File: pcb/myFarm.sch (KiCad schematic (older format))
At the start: 10 parts, among them J0 Conn_01x02, J1 LED, J2 SENSOR, J3 SW_LED, J4 RELAY, J5 POWER DRIVE, J6 JUMPER, J7 SW_LED, U1 WeMos_D1_mini, U2 MCP23017_MODULE

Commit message: update pcb
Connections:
- wire segments 80 -> 82
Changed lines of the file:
@@
 EESchema Schematic File Version 4
 LIBS:myFarm-cache
-EELAYER 29 0
+EELAYER 30 0
 EELAYER END
 $Descr A4 11693 8268
@@
 	3600 5400 3250 5400
 Wire Wire Line
-	3250 5500 3500 5500
-Wire Wire Line
 	3500 6300 3500 6050
 Wire Wire Line
@@
 	1650 4150 1650 2900
 Wire Wire Line
-	1650 2900 2800 2900
+	1650 2900 2150 2900
 Connection ~ 2800 2900
 Wire Wire Line
@@
 	3650 3250 3500 3250
 Wire Wire Line
-	3500 3250 3500 5500
-Connection ~ 3500 5500
-Wire Wire Line
-	3500 5500 3500 6050
-Wire Wire Line
 	3650 3050 3500 3050
 Wire Wire Line
@@
 	0    1    1    0
 $EndComp
+Wire Wire Line
+	3500 3250 3500 6050
+Wire Wire Line
+	3250 5500 3250 5750
+Wire Wire Line
+	3250 5750 2150 5750
+Wire Wire Line
+	2150 5750 2150 2900
+Connection ~ 2150 2900
+Wire Wire Line
+	2150 2900 2800 2900
 $EndSCHEMATC

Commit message: update pcb
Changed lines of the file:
@@
 	3100 3950 3250 3950
 Wire Wire Line
-	3250 3950 3250 5300
-Wire Wire Line
 	3850 4550 3600 4550
-Wire Wire Line
-	3600 4550 3600 5400
-Wire Wire Line
-	3600 5400 3250 5400
 Wire Wire Line
 	3500 6300 3500 6050
@@
 Wire Wire Line
 	1650 4150 1650 2900
-Wire Wire Line
-	1650 2900 2150 2900
 Connection ~ 2800 2900
 Wire Wire Line
@@
 	1550 2850 1550 4000
 Connection ~ 1550 4000
+Connection ~ 5900 3350
+Wire Wire Line
+	5900 3350 5900 3750
+Wire Wire Line
+	5900 3350 5900 3000
+Wire Wire Line
+	5650 3550 6300 3550
+Wire Wire Line
+	6300 3350 5900 3350
+Wire Wire Line
+	3500 3050 3500 2900
+Connection ~ 3500 2900
+Wire Wire Line
+	3500 2900 4550 2900
+$Comp
+L Connector_Generic:Conn_01x04 J7
+U 1 1 5D3E2091
+P 1550 4350
+F 0 "J7" V 1422 4530 50  0000 L CNN
+F 1 "SW_LED" V 1513 4530 50  0000 L CNN
+F 2 "Module:POWER_SUPPLY_MODULE" H 1550 4350 50  0001 C CNN
+F 3 "~" H 1550 4350 50  0001 C CNN
+	1    1550 4350
+	0    1    1    0
+$EndComp
+Wire Wire Line
+	3500 3250 3500 6050
+Wire Wire Line
+	3100 4150 3350 4150
+Wire Wire Line
+	3350 4150 3350 3150
+Wire Wire Line
+	3650 3050 3500 3050
+Wire Wire Line
+	3350 3150 3650 3150
+Wire Wire Line
+	3650 3250 3500 3250
 $Comp
 L Connector_Generic:Conn_01x03 J6
@@
 	-1   0    0    1
 $EndComp
-Connection ~ 5900 3350
-Wire Wire Line
-	5900 3350 5900 3750
-Wire Wire Line
-	5900 3350 5900 3000
-Wire Wire Line
-	5650 3550 6300 3550
-Wire Wire Line
-	6300 3350 5900 3350
+Wire Wire Line
+	3250 3950 3250 5300
+Wire Wire Line
+	3600 4550 3600 5400
+Wire Wire Line
+	3600 5400 3250 5400
+Wire Wire Line
+	3250 5500 3250 5750
+Wire Wire Line
+	3250 5750 2150 5750
+Wire Wire Line
+	2150 2900 2800 2900
+Wire Wire Line
+	1650 2900 2150 2900
+Connection ~ 2150 2900
+Wire Wire Line
+	2150 5750 2150 2900
 $Comp
 L Connector_Generic:Conn_01x03 J2
@@
 	1    0    0    -1
 $EndComp
-Wire Wire Line
-	3650 3250 3500 3250
-Wire Wire Line
-	3650 3050 3500 3050
-Wire Wire Line
-	3500 3050 3500 2900
-Connection ~ 3500 2900
-Wire Wire Line
-	3500 2900 4550 2900
-Wire Wire Line
-	3100 3650 3250 3650
-Wire Wire Line
-	3250 3650 3250 3150
-Wire Wire Line
-	3250 3150 3650 3150
-$Comp
-L Connector_Generic:Conn_01x04 J7
-U 1 1 5D3E2091
-P 1550 4350
-F 0 "J7" V 1422 4530 50  0000 L CNN
-F 1 "SW_LED" V 1513 4530 50  0000 L CNN
-F 2 "Module:POWER_SUPPLY_MODULE" H 1550 4350 50  0001 C CNN
-F 3 "~" H 1550 4350 50  0001 C CNN
-	1    1550 4350
-	0    1    1    0
-$EndComp
-Wire Wire Line
-	3500 3250 3500 6050
-Wire Wire Line
-	3250 5500 3250 5750
-Wire Wire Line
-	3250 5750 2150 5750
-Wire Wire Line
-	2150 5750 2150 2900
-Connection ~ 2150 2900
-Wire Wire Line
-	2150 2900 2800 2900
 $EndSCHEMATC

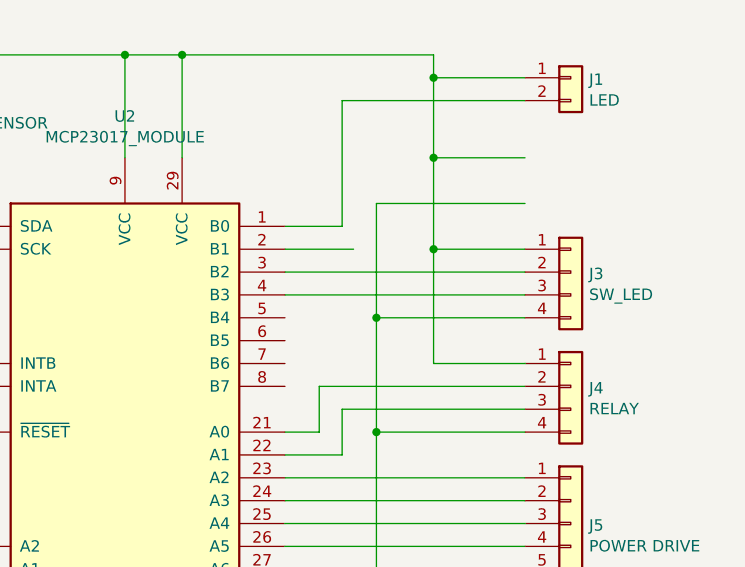
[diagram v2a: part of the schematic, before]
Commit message: swap connect j3
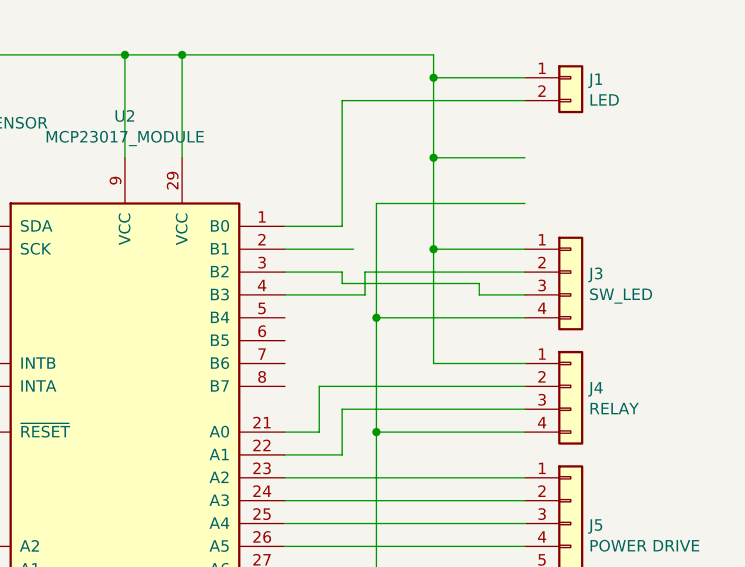
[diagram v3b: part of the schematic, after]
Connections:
- wire segments 82 -> 88
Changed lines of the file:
@@
 	5500 3100 6300 3100
-Wire Wire Line
-	5250 3850 6300 3850
-Wire Wire Line
-	5250 3950 6300 3950
 Wire Wire Line
 	5250 4550 5400 4550
@@
 	1    0    0    -1
 $EndComp
+Wire Wire Line
+	5250 3950 5600 3950
+Wire Wire Line
+	5600 3950 5600 3850
+Wire Wire Line
+	5600 3850 6300 3850
+Wire Wire Line
+	5250 3850 5500 3850
+Wire Wire Line
+	5500 3850 5500 3900
+Wire Wire Line
+	5500 3900 6100 3900
+Wire Wire Line
+	6100 3900 6100 3950
+Wire Wire Line
+	6100 3950 6300 3950
 $EndSCHEMATC

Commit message: update pcb
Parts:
- added J10: GENERAL, Connector_PinHeader_2.54mm:PinHeader_1x06_P2.54mm_Vertical, symbol Connector_Generic:Conn_01x06
- added J11: RXTX, Connector_PinHeader_2.54mm:PinHeader_1x02_P2.54mm_Vertical, symbol Connector_Generic:Conn_01x02
- added J12, J13, J14: VALVE OUT, Connector_PinHeader_2.54mm:PinHeader_1x02_P2.54mm_Vertical, symbol Connector_Generic:Conn_01x02
- added J8: Reset, Connector_PinHeader_2.54mm:PinHeader_1x02_P2.54mm_Vertical, symbol Connector_Generic:Conn_01x02
- added J9: VAVLE IN, Connector_PinHeader_2.54mm:PinHeader_1x02_P2.54mm_Vertical, symbol Connector_Generic:Conn_01x02
- added U3: DS1832S+, Package_DIP:DIP-8_W10.16mm, symbol DS1832S_:DS1832S+
- J0: value Conn_01x02 -> POWER
- J7: value SW_LED -> SUPPLY
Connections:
- wire segments 88 -> 150
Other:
- moved on the sheet: J0, J1, J2, J3, J4, J5, J6, J7, U1, U2

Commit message: update pcb.
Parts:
- added J15: SELECTOR, Connector_PinHeader_2.54mm:PinHeader_1x02_P2.54mm_Vertical, symbol Connector_Generic:Conn_01x02
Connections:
- net GNDREF: now also J15.1 (Pin_1)
- net at U1.11 (D4): now also J15.2 (Pin_2)
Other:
- moved on the sheet: J6
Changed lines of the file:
@@
 	5450 4500 5450 5700
 Wire Wire Line
-	5450 5700 6250 5700
+	5450 5700 6000 5700
 Wire Wire Line
 	7300 5200 7300 5700
@@
 Wire Wire Line
 	7300 2550 7550 2550
-Wire Wire Line
-	5850 3600 6000 3600
-Wire Wire Line
-	6600 4200 6350 4200
 Wire Wire Line
 	6250 5950 6250 5700
@@
 	8000 4900 9050 4900
 Connection ~ 5550 2550
-$Comp
-L Connector_Generic:Conn_01x03 J6
-U 1 1 5D3BA3DB
-P 5800 5050
-F 0 "J6" H 5718 4725 50  0000 C CNN
-F 1 "JUMPER" H 5718 4816 50  0000 C CNN
-F 2 "Connector_PinHeader_2.54mm:PinHeader_1x03_P2.54mm_Vertical" H 5800 5050 50  0001 C CNN
-F 3 "~" H 5800 5050 50  0001 C CNN
-	1    5800 5050
-	-1   0    0    1
-$EndComp
-Wire Wire Line
-	6350 4200 6350 5050
-Wire Wire Line
-	6350 5050 6000 5050
-Wire Wire Line
-	6000 5150 6000 5400
-Wire Wire Line
-	6000 5400 4900 5400
-Wire Wire Line
-	4900 2550 5550 2550
-Wire Wire Line
-	4900 5400 4900 2550
 Wire Wire Line
 	8000 3600 8350 3600
@@
 Wire Wire Line
 	3400 1700 4050 1700
-Connection ~ 4900 2550
 Wire Wire Line
 	4250 4250 4250 5700
@@
 Wire Wire Line
 	4250 3450 4250 2550
-Wire Wire Line
-	4250 2550 4900 2550
 Wire Wire Line
 	4400 3850 4400 3300
@@
 Wire Wire Line
 	3300 1700 3300 1850
-Wire Wire Line
-	6000 3600 6000 4950
 Wire Wire Line
 	5850 3900 6150 3900
@@
 	6850 2800 6850 1800
 Wire Wire Line
-	6550 3800 6550 2800
-Wire Wire Line
-	6550 2800 6850 2800
-Wire Wire Line
-	5850 3800 6550 3800
+	6450 3800 6450 2800
+Wire Wire Line
+	6450 2800 6850 2800
+Wire Wire Line
+	5850 3800 6450 3800
 Wire Wire Line
 	6000 1800 6000 3200
@@
 Connection ~ 6400 2550
 Wire Wire Line
-	6400 2550 6750 2550
+	6400 2550 6550 2550
 Wire Wire Line
 	6500 1800 6500 2200
@@
 	8650 2450 9050 2450
 $Comp
+L Connector_Generic:Conn_01x02 J9
+U 1 1 5D6744E9
+P 7700 1600
+F 0 "J9" H 7780 1592 50  0000 L CNN
+F 1 "VAVLE IN" H 7780 1501 50  0000 L CNN
+F 2 "Connector_PinHeader_2.54mm:PinHeader_1x02_P2.54mm_Vertical" H 7700 1600 50  0001 C CNN
+F 3 "~" H 7700 1600 50  0001 C CNN
+	1    7700 1600
+	0    -1   -1   0
+$EndComp
+$Comp
+L Connector_Generic:Conn_01x02 J12
+U 1 1 5D67486F
+P 8000 1600
+F 0 "J12" H 8080 1592 50  0000 L CNN
+F 1 "VALVE OUT" H 8080 1501 50  0000 L CNN
+F 2 "Connector_PinHeader_2.54mm:PinHeader_1x02_P2.54mm_Vertical" H 8000 1600 50  0001 C CNN
+F 3 "~" H 8000 1600 50  0001 C CNN
+	1    8000 1600
+	0    -1   -1   0
+$EndComp
+$Comp
+L Connector_Generic:Conn_01x02 J13
+U 1 1 5D6923CB
+P 8300 1600
+F 0 "J13" H 8380 1592 50  0000 L CNN
+F 1 "VALVE OUT" H 8380 1501 50  0000 L CNN
+F 2 "Connector_PinHeader_2.54mm:PinHeader_1x02_P2.54mm_Vertical" H 8300 1600 50  0001 C CNN
+F 3 "~" H 8300 1600 50  0001 C CNN
+	1    8300 1600
+	0    -1   -1   0
+$EndComp
+$Comp
+L Connector_Generic:Conn_01x02 J14
+U 1 1 5D692989
+P 8600 1600
+F 0 "J14" H 8680 1592 50  0000 L CNN
+F 1 "VALVE OUT" H 8680 1501 50  0000 L CNN
+F 2 "Connector_PinHeader_2.54mm:PinHeader_1x02_P2.54mm_Vertical" H 8600 1600 50  0001 C CNN
+F 3 "~" H 8600 1600 50  0001 C CNN
+	1    8600 1600
+	0    -1   -1   0
+$EndComp
+Wire Wire Line
+	8050 2100 7700 2100
+Wire Wire Line
+	7700 2100 7700 1800
+Wire Wire Line
+	8050 2100 8050 3700
+Wire Wire Line
+	8100 2000 8000 2000
+Wire Wire Line
+	8000 2000 8000 1800
+Wire Wire Line
+	8100 2000 8100 3800
+Wire Wire Line
+	8150 2000 8300 2000
+Wire Wire Line
+	8300 2000 8300 1800
+Wire Wire Line
+	8150 2000 8150 3900
+Wire Wire Line
+	8200 2100 8600 2100
+Wire Wire Line
+	8600 2100 8600 1800
+Wire Wire Line
+	8200 2100 8200 4000
+Wire Wire Line
+	7800 1800 7800 1950
+Wire Wire Line
+	7800 1950 8100 1950
+Wire Wire Line
+	8700 1950 8700 2200
+Wire Wire Line
+	8700 2200 8400 2200
+Connection ~ 8400 2200
+Wire Wire Line
+	8700 1800 8700 1950
+Connection ~ 8700 1950
+Wire Wire Line
+	8400 1800 8400 1950
+Connection ~ 8400 1950
+Wire Wire Line
+	8400 1950 8700 1950
+Wire Wire Line
+	8100 1800 8100 1950
+Connection ~ 8100 1950
+Wire Wire Line
+	8100 1950 8400 1950
+$Comp
+L Connector_Generic:Conn_01x03 J6
+U 1 1 5D3BA3DB
+P 6450 4500
+F 0 "J6" H 6368 4175 50  0000 C CNN
+F 1 "JUMPER" H 6368 4266 50  0000 C CNN
+F 2 "Connector_PinHeader_2.54mm:PinHeader_1x03_P2.54mm_Vertical" H 6450 4500 50  0001 C CNN
+F 3 "~" H 6450 4500 50  0001 C CNN
+	1    6450 4500
+	0    1    1    0
+$EndComp
+Wire Wire Line
+	6600 4200 6450 4200
+Wire Wire Line
+	6450 4200 6450 4300
+Wire Wire Line
+	6350 3600 6350 4300
+Wire Wire Line
+	6550 4300 6550 2550
+Connection ~ 6550 2550
+Wire Wire Line
+	6550 2550 6750 2550
+Wire Wire Line
+	5850 3600 6350 3600
+Wire Wire Line
+	4250 2550 5550 2550
+$Comp
+L Connector_Generic:Conn_01x02 J15
+U 1 1 5D75F2CC
+P 5700 5300
+F 0 "J15" H 5780 5292 50  0000 L CNN
+F 1 "SELECTOR" H 5780 5201 50  0000 L CNN
+F 2 "Connector_PinHeader_2.54mm:PinHeader_1x02_P2.54mm_Vertical" H 5700 5300 50  0001 C CNN
+F 3 "~" H 5700 5300 50  0001 C CNN
+	1    5700 5300
+	-1   0    0    1
+$EndComp
+Wire Wire Line
+	5850 3700 6000 3700
+Wire Wire Line
+	6000 3700 6000 5200
+Wire Wire Line
+	6000 5200 5900 5200
+Wire Wire Line
+	5900 5300 6000 5300
+Wire Wire Line
+	6000 5300 6000 5700
+Connection ~ 6000 5700
+Wire Wire Line
+	6000 5700 6250 5700
+$Comp
 L Connector_Generic:Conn_01x02 J1
 U 1 1 5D3273EB
@@
 	1    0    0    -1
 $EndComp
-$Comp
-L Connector_Generic:Conn_01x02 J9
-U 1 1 5D6744E9
-P 7700 1600
-F 0 "J9" H 7780 1592 50  0000 L CNN
-F 1 "VAVLE IN" H 7780 1501 50  0000 L CNN
-F 2 "Connector_PinHeader_2.54mm:PinHeader_1x02_P2.54mm_Vertical" H 7700 1600 50  0001 C CNN
-F 3 "~" H 7700 1600 50  0001 C CNN
-	1    7700 1600
-	0    -1   -1   0
-$EndComp
-$Comp
-L Connector_Generic:Conn_01x02 J12
-U 1 1 5D67486F
-P 8000 1600
-F 0 "J12" H 8080 1592 50  0000 L CNN
-F 1 "VALVE OUT" H 8080 1501 50  0000 L CNN
-F 2 "Connector_PinHeader_2.54mm:PinHeader_1x02_P2.54mm_Vertical" H 8000 1600 50  0001 C CNN
-F 3 "~" H 8000 1600 50  0001 C CNN
-	1    8000 1600
-	0    -1   -1   0
-$EndComp
-$Comp
-L Connector_Generic:Conn_01x02 J13
-U 1 1 5D6923CB
-P 8300 1600
-F 0 "J13" H 8380 1592 50  0000 L CNN
-F 1 "VALVE OUT" H 8380 1501 50  0000 L CNN
-F 2 "Connector_PinHeader_2.54mm:PinHeader_1x02_P2.54mm_Vertical" H 8300 1600 50  0001 C CNN
-F 3 "~" H 8300 1600 50  0001 C CNN
-	1    8300 1600
-	0    -1   -1   0
-$EndComp
-$Comp
-L Connector_Generic:Conn_01x02 J14
-U 1 1 5D692989
-P 8600 1600
-F 0 "J14" H 8680 1592 50  0000 L CNN
-F 1 "VALVE OUT" H 8680 1501 50  0000 L CNN
-F 2 "Connector_PinHeader_2.54mm:PinHeader_1x02_P2.54mm_Vertical" H 8600 1600 50  0001 C CNN
-F 3 "~" H 8600 1600 50  0001 C CNN
-	1    8600 1600
-	0    -1   -1   0
-$EndComp
-Wire Wire Line
-	8050 2100 7700 2100
-Wire Wire Line
-	7700 2100 7700 1800
-Wire Wire Line
-	8050 2100 8050 3700
-Wire Wire Line
-	8100 2000 8000 2000
-Wire Wire Line
-	8000 2000 8000 1800
-Wire Wire Line
-	8100 2000 8100 3800
-Wire Wire Line
-	8150 2000 8300 2000
-Wire Wire Line
-	8300 2000 8300 1800
-Wire Wire Line
-	8150 2000 8150 3900
-Wire Wire Line
-	8200 2100 8600 2100
-Wire Wire Line
-	8600 2100 8600 1800
-Wire Wire Line
-	8200 2100 8200 4000
-Wire Wire Line
-	7800 1800 7800 1950
-Wire Wire Line
-	7800 1950 8100 1950
-Wire Wire Line
-	8700 1950 8700 2200
-Wire Wire Line
-	8700 2200 8400 2200
-Connection ~ 8400 2200
-Wire Wire Line
-	8700 1800 8700 1950
-Connection ~ 8700 1950
-Wire Wire Line
-	8400 1800 8400 1950
-Connection ~ 8400 1950
-Wire Wire Line
-	8400 1950 8700 1950
-Wire Wire Line
-	8100 1800 8100 1950
-Connection ~ 8100 1950
-Wire Wire Line
-	8100 1950 8400 1950
 $EndSCHEMATC

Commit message: update pcb.
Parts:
- J5: footprint Connector_PinHeader_2.54mm:PinHeader_1x06_P2.54mm_Vertical -> Connector_PinHeader_2.54mm:PinHeader_1x08_P2.54mm_Vertical; symbol Connector_Generic:Conn_01x06 -> Connector_Generic:Conn_01x08
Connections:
- net GNDREF: now also J5.8 (Pin_8)
- net at J1.1 (Pin_1), J10.5 (Pin_5), J2.1 (Pin_1)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: now also J5.7 (Pin_7)
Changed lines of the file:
@@
 $EndComp
 $Comp
-L Connector_Generic:Conn_01x06 J5
+L Connector_Generic:Conn_01x08 J5
 U 1 1 5D328442
-P 9250 4600
-F 0 "J5" H 9330 4592 50  0000 L CNN
-F 1 "POWER DRIVE" H 9330 4501 50  0000 L CNN
-F 2 "Connector_PinHeader_2.54mm:PinHeader_1x06_P2.54mm_Vertical" H 9250 4600 50  0001 C CNN
-F 3 "~" H 9250 4600 50  0001 C CNN
-	1    9250 4600
+P 9250 4700
+F 0 "J5" H 9330 4692 50  0000 L CNN
+F 1 "POWER DRIVE" H 9330 4601 50  0000 L CNN
+F 2 "Connector_PinHeader_2.54mm:PinHeader_1x08_P2.54mm_Vertical" H 9250 4700 50  0001 C CNN
+F 3 "~" H 9250 4700 50  0001 C CNN
+	1    9250 4700
 	1    0    0    -1
 $EndComp
@@
 	7550 5700 8400 5700
 Wire Wire Line
-	8400 5700 8400 4200
+	8400 5700 8400 5100
 Connection ~ 7550 5700
 Wire Wire Line
@@
 	1    0    0    -1
 $EndComp
+Wire Wire Line
+	9050 5100 8400 5100
+Connection ~ 8400 5100
+Wire Wire Line
+	8400 5100 8400 4200
+Wire Wire Line
+	8650 3900 8650 5000
+Wire Wire Line
+	8650 5000 9050 5000
+Connection ~ 8650 3900
 $EndSCHEMATC

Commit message: update pcb
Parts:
- J0: footprint Connector_PinHeader_2.54mm:PinHeader_1x02_P2.54mm_Horizontal -> Connector_JST:JST_XH_B2B-XH-A_1x02_P2.50mm_Vertical
- J1, J11, J12, J13, J14, J15, J8, J9: footprint Connector_PinHeader_2.54mm:PinHeader_1x02_P2.54mm_Vertical -> Connector_JST:JST_XH_B2B-XH-A_1x02_P2.50mm_Vertical
- J10: footprint Connector_PinHeader_2.54mm:PinHeader_1x06_P2.54mm_Vertical -> Connector_JST:JST_XH_B6B-XH-A_1x06_P2.50mm_Vertical
- J2: footprint Connector_PinHeader_2.54mm:PinHeader_1x03_P2.54mm_Vertical -> Connector_JST:JST_XH_B3B-XH-A_1x03_P2.50mm_Vertical
- J3, J4: footprint Connector_PinHeader_2.54mm:PinHeader_1x04_P2.54mm_Vertical -> Connector_JST:JST_XH_B4B-XH-A_1x04_P2.50mm_Vertical
- J5: footprint Connector_PinHeader_2.54mm:PinHeader_1x08_P2.54mm_Vertical -> Connector_JST:JST_XH_B8B-XH-A_1x08_P2.50mm_Vertical
- J7: footprint Module:POWER_SUPPLY_MODULE -> Connector_JST:JST_XH_B4B-XH-A_1x04_P2.50mm_Vertical
- U3: footprint Package_DIP:DIP-8_W10.16mm -> Package_DIP:DIP-8_W7.62mm_Socket
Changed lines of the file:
@@
 EESchema Schematic File Version 4
-LIBS:myFarm-cache
 EELAYER 30 0
 EELAYER END
@@
 F 0 "J3" H 9330 3492 50  0000 L CNN
 F 1 "SW_LED" H 9330 3401 50  0000 L CNN
-F 2 "Connector_PinHeader_2.54mm:PinHeader_1x04_P2.54mm_Vertical" H 9250 3500 50  0001 C CNN
+F 2 "Connector_JST:JST_XH_B4B-XH-A_1x04_P2.50mm_Vertical" H 9250 3500 50  0001 C CNN
 F 3 "~" H 9250 3500 50  0001 C CNN
 	1    9250 3500
@@
 F 0 "J5" H 9330 4692 50  0000 L CNN
 F 1 "POWER DRIVE" H 9330 4601 50  0000 L CNN
-F 2 "Connector_PinHeader_2.54mm:PinHeader_1x08_P2.54mm_Vertical" H 9250 4700 50  0001 C CNN
+F 2 "Connector_JST:JST_XH_B8B-XH-A_1x08_P2.50mm_Vertical" H 9250 4700 50  0001 C CNN
 F 3 "~" H 9250 4700 50  0001 C CNN
 	1    9250 4700
@@
 F 0 "J0" V 3164 1262 50  0000 R CNN
 F 1 "POWER" V 3073 1262 50  0000 R CNN
-F 2 "Connector_PinHeader_2.54mm:PinHeader_1x02_P2.54mm_Horizontal" H 3200 1450 50  0001 C CNN
+F 2 "Connector_JST:JST_XH_B2B-XH-A_1x02_P2.50mm_Vertical" H 3200 1450 50  0001 C CNN
 F 3 "~" H 3200 1450 50  0001 C CNN
 	1    3200 1450
@@
 F 0 "J4" H 9330 3992 50  0000 L CNN
 F 1 "RELAY" H 9330 3901 50  0000 L CNN
-F 2 "Connector_PinHeader_2.54mm:PinHeader_1x04_P2.54mm_Vertical" H 9250 4000 50  0001 C CNN
+F 2 "Connector_JST:JST_XH_B4B-XH-A_1x04_P2.50mm_Vertical" H 9250 4000 50  0001 C CNN
 F 3 "~" H 9250 4000 50  0001 C CNN
 	1    9250 4000
@@
 F 0 "J8" H 2368 3325 50  0000 C CNN
 F 1 "Reset" H 2368 3416 50  0000 C CNN
-F 2 "Connector_PinHeader_2.54mm:PinHeader_1x02_P2.54mm_Vertical" H 2450 3650 50  0001 C CNN
+F 2 "Connector_JST:JST_XH_B2B-XH-A_1x02_P2.50mm_Vertical" H 2450 3650 50  0001 C CNN
 F 3 "~" H 2450 3650 50  0001 C CNN
 	1    2450 3650
@@
 F 0 "J7" V 3172 2230 50  0000 L CNN
 F 1 "SUPPLY" V 3263 2230 50  0000 L CNN
-F 2 "Module:POWER_SUPPLY_MODULE" H 3300 2050 50  0001 C CNN
+F 2 "Connector_JST:JST_XH_B4B-XH-A_1x04_P2.50mm_Vertical" H 3300 2050 50  0001 C CNN
 F 3 "~" H 3300 2050 50  0001 C CNN
 	1    3300 2050
@@
 F 0 "J10" H 6280 1592 50  0000 L CNN
 F 1 "GENERAL" H 6280 1501 50  0000 L CNN
-F 2 "Connector_PinHeader_2.54mm:PinHeader_1x06_P2.54mm_Vertical" H 6200 1600 50  0001 C CNN
+F 2 "Connector_JST:JST_XH_B6B-XH-A_1x06_P2.50mm_Vertical" H 6200 1600 50  0001 C CNN
 F 3 "~" H 6200 1600 50  0001 C CNN
 	1    6200 1600
@@
 	6500 2200 6950 2200
 Connection ~ 6950 2200
-$Comp
-L Connector_Generic:Conn_01x02 J11
-U 1 1 5D80D919
-P 4650 1950
-F 0 "J11" H 4568 1625 50  0000 C CNN
-F 1 "RXTX" H 4568 1716 50  0000 C CNN
-F 2 "Connector_PinHeader_2.54mm:PinHeader_1x02_P2.54mm_Vertical" H 4650 1950 50  0001 C CNN
-F 3 "~" H 4650 1950 50  0001 C CNN
-	1    4650 1950
-	0    -1   -1   0
-$EndComp
 Wire Wire Line
 	4050 1700 4050 2550
@@
 F 0 "U3" H 3550 4517 50  0000 C CNN
 F 1 "DS1832S+" H 3550 4426 50  0000 C CNN
-F 2 "Package_DIP:DIP-8_W10.16mm" H 3550 3850 50  0001 L BNN
+F 2 "Package_DIP:DIP-8_W7.62mm_Socket" H 3550 3850 50  0001 L BNN
 F 3 "" H 3550 3850 50  0001 L BNN
 F 4 "IPC7351B" H 3550 3850 50  0001 L BNN "Field4"
@@
 F 0 "J2" H 6930 1642 50  0000 L CNN
 F 1 "SENSOR" H 6930 1551 50  0000 L CNN
-F 2 "Connector_PinHeader_2.54mm:PinHeader_1x03_P2.54mm_Vertical" H 6850 1600 50  0001 C CNN
+F 2 "Connector_JST:JST_XH_B3B-XH-A_1x03_P2.50mm_Vertical" H 6850 1600 50  0001 C CNN
 F 3 "~" H 6850 1600 50  0001 C CNN
 	1    6850 1600
@@
 F 0 "J9" H 7780 1592 50  0000 L CNN
 F 1 "VAVLE IN" H 7780 1501 50  0000 L CNN
-F 2 "Connector_PinHeader_2.54mm:PinHeader_1x02_P2.54mm_Vertical" H 7700 1600 50  0001 C CNN
+F 2 "Connector_JST:JST_XH_B2B-XH-A_1x02_P2.50mm_Vertical" H 7700 1600 50  0001 C CNN
 F 3 "~" H 7700 1600 50  0001 C CNN
 	1    7700 1600
@@
 F 0 "J12" H 8080 1592 50  0000 L CNN
 F 1 "VALVE OUT" H 8080 1501 50  0000 L CNN
-F 2 "Connector_PinHeader_2.54mm:PinHeader_1x02_P2.54mm_Vertical" H 8000 1600 50  0001 C CNN
+F 2 "Connector_JST:JST_XH_B2B-XH-A_1x02_P2.50mm_Vertical" H 8000 1600 50  0001 C CNN
 F 3 "~" H 8000 1600 50  0001 C CNN
 	1    8000 1600
@@
 F 0 "J13" H 8380 1592 50  0000 L CNN
 F 1 "VALVE OUT" H 8380 1501 50  0000 L CNN
-F 2 "Connector_PinHeader_2.54mm:PinHeader_1x02_P2.54mm_Vertical" H 8300 1600 50  0001 C CNN
+F 2 "Connector_JST:JST_XH_B2B-XH-A_1x02_P2.50mm_Vertical" H 8300 1600 50  0001 C CNN
 F 3 "~" H 8300 1600 50  0001 C CNN
 	1    8300 1600
@@
 F 0 "J14" H 8680 1592 50  0000 L CNN
 F 1 "VALVE OUT" H 8680 1501 50  0000 L CNN
-F 2 "Connector_PinHeader_2.54mm:PinHeader_1x02_P2.54mm_Vertical" H 8600 1600 50  0001 C CNN
+F 2 "Connector_JST:JST_XH_B2B-XH-A_1x02_P2.50mm_Vertical" H 8600 1600 50  0001 C CNN
 F 3 "~" H 8600 1600 50  0001 C CNN
 	1    8600 1600
@@
 F 0 "J15" H 5780 5292 50  0000 L CNN
 F 1 "SELECTOR" H 5780 5201 50  0000 L CNN
-F 2 "Connector_PinHeader_2.54mm:PinHeader_1x02_P2.54mm_Vertical" H 5700 5300 50  0001 C CNN
+F 2 "Connector_JST:JST_XH_B2B-XH-A_1x02_P2.50mm_Vertical" H 5700 5300 50  0001 C CNN
 F 3 "~" H 5700 5300 50  0001 C CNN
 	1    5700 5300
@@
 F 0 "J1" H 9330 2442 50  0000 L CNN
 F 1 "LED" H 9330 2351 50  0000 L CNN
-F 2 "Connector_PinHeader_2.54mm:PinHeader_1x02_P2.54mm_Vertical" H 9250 2450 50  0001 C CNN
+F 2 "Connector_JST:JST_XH_B2B-XH-A_1x02_P2.50mm_Vertical" H 9250 2450 50  0001 C CNN
 F 3 "~" H 9250 2450 50  0001 C CNN
 	1    9250 2450
@@
 	8650 5000 9050 5000
 Connection ~ 8650 3900
+$Comp
+L Connector_Generic:Conn_01x02 J11
+U 1 1 5D80D919
+P 4650 1950
+F 0 "J11" H 4568 1625 50  0000 C CNN
+F 1 "RXTX" H 4568 1716 50  0000 C CNN
+F 2 "Connector_JST:JST_XH_B2B-XH-A_1x02_P2.50mm_Vertical" H 4650 1950 50  0001 C CNN
+F 3 "~" H 4650 1950 50  0001 C CNN
+	1    4650 1950
+	0    -1   -1   0
+$EndComp
 $EndSCHEMATC
